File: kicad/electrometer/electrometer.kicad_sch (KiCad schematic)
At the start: 6 parts, among them J1 Screw_Terminal_01x04, U1 LMC6082

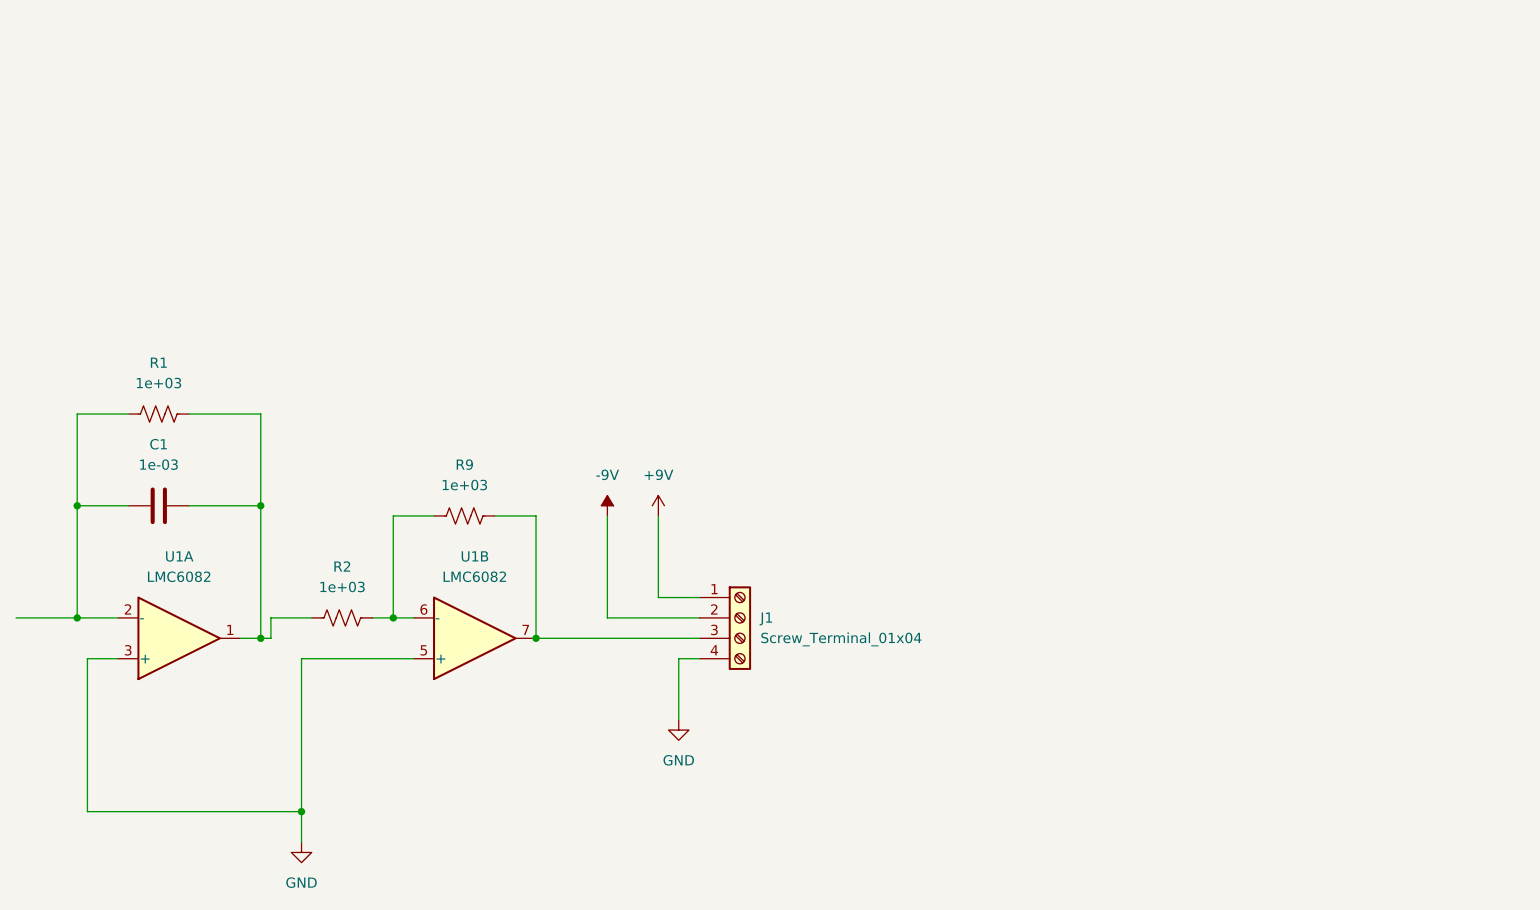
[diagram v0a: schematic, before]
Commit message: moved around some kicad things. Added additional schematic for ADC and TPS60213
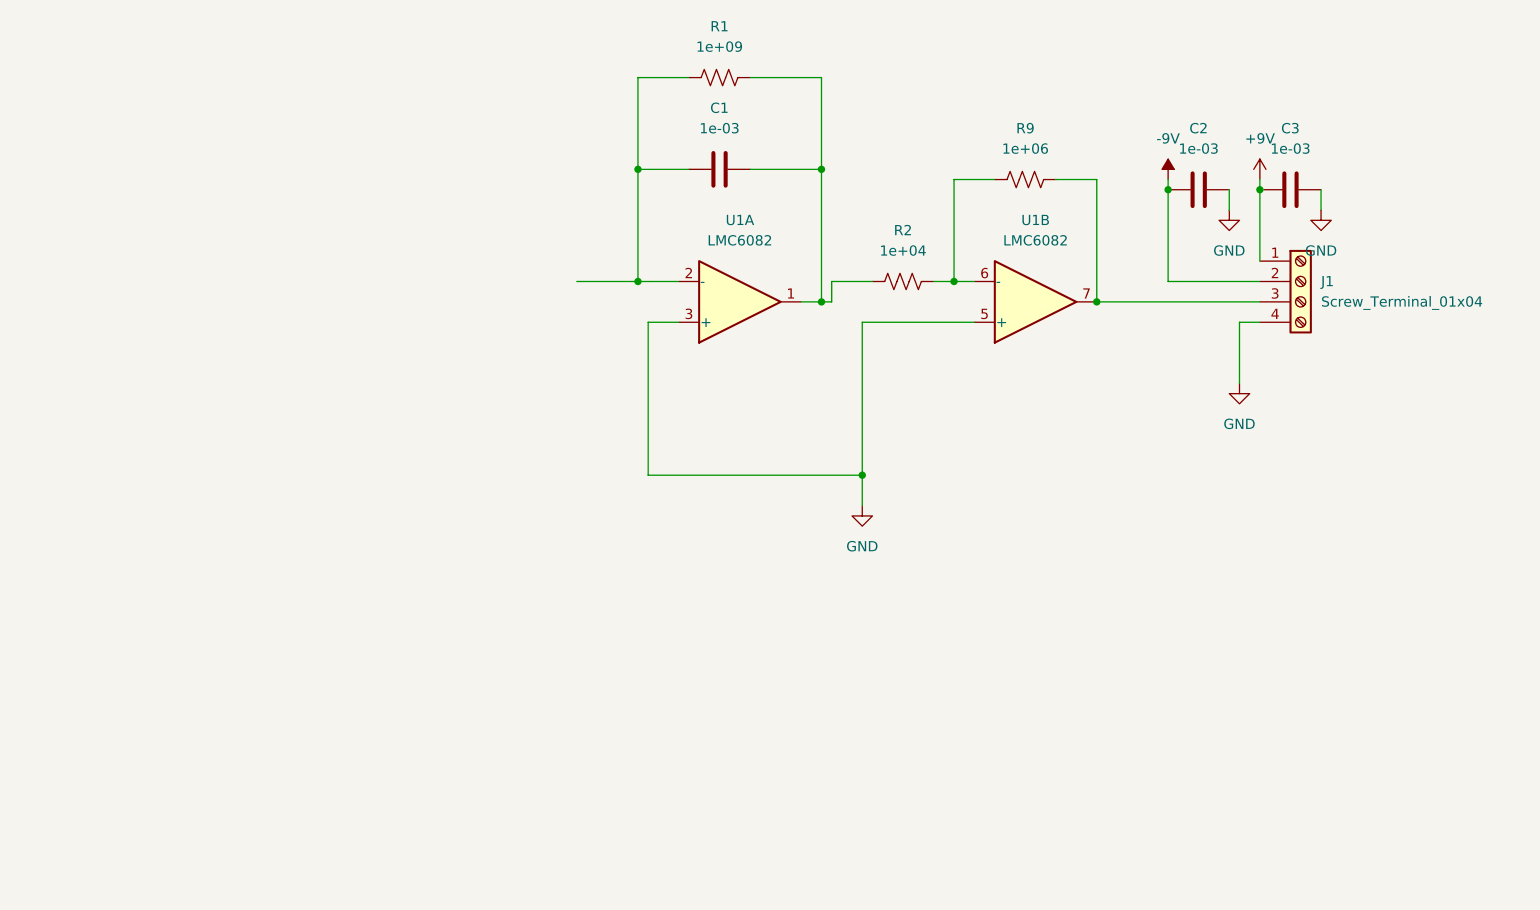
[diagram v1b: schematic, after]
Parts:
- added C2, C3: 1e-03, Capacitor_SMD:C_1206_3216Metric_Pad1.33x1.80mm_HandSolder, symbol Device:C
- C1: footprint Capacitor_SMD:C_1206_3216Metric_Pad1.33x1.80mm_HandSolder -> Capacitor_THT:C_Disc_D3.0mm_W1.6mm_P2.50mm
- R1: value 1e+03 -> 1e+09; footprint Resistor_SMD:R_1206_3216Metric_Pad1.30x1.75mm_HandSolder -> Resistor_THT:R_Axial_DIN0204_L3.6mm_D1.6mm_P2.54mm_Vertical
- R2: value 1e+03 -> 1e+04
- R9: value 1e+03 -> 1e+06
- U1: footprint Package_DIP:DIP-8-16_W7.62mm -> Package_DIP:DIP-8_W7.62mm
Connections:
- net +9V: now also C3.1
- net -9V: now also C2.1
- net GND: now also C2.2, C3.2
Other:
- moved on the sheet: C1, J1, R1, R2, R9, U1A, U1B
